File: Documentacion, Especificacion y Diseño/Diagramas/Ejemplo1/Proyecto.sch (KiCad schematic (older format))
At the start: 12 parts

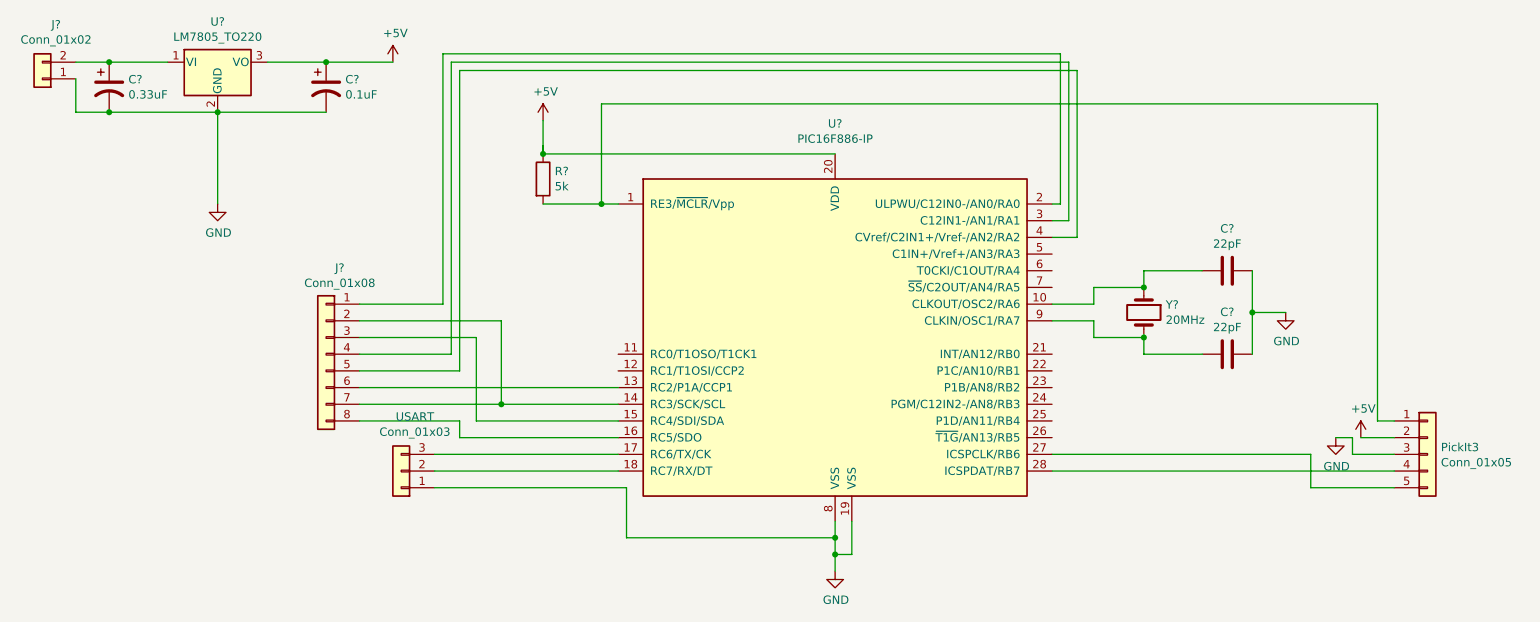
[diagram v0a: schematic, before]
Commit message: Tratado de hacer parte del circuito sin cruces y con especificaciones
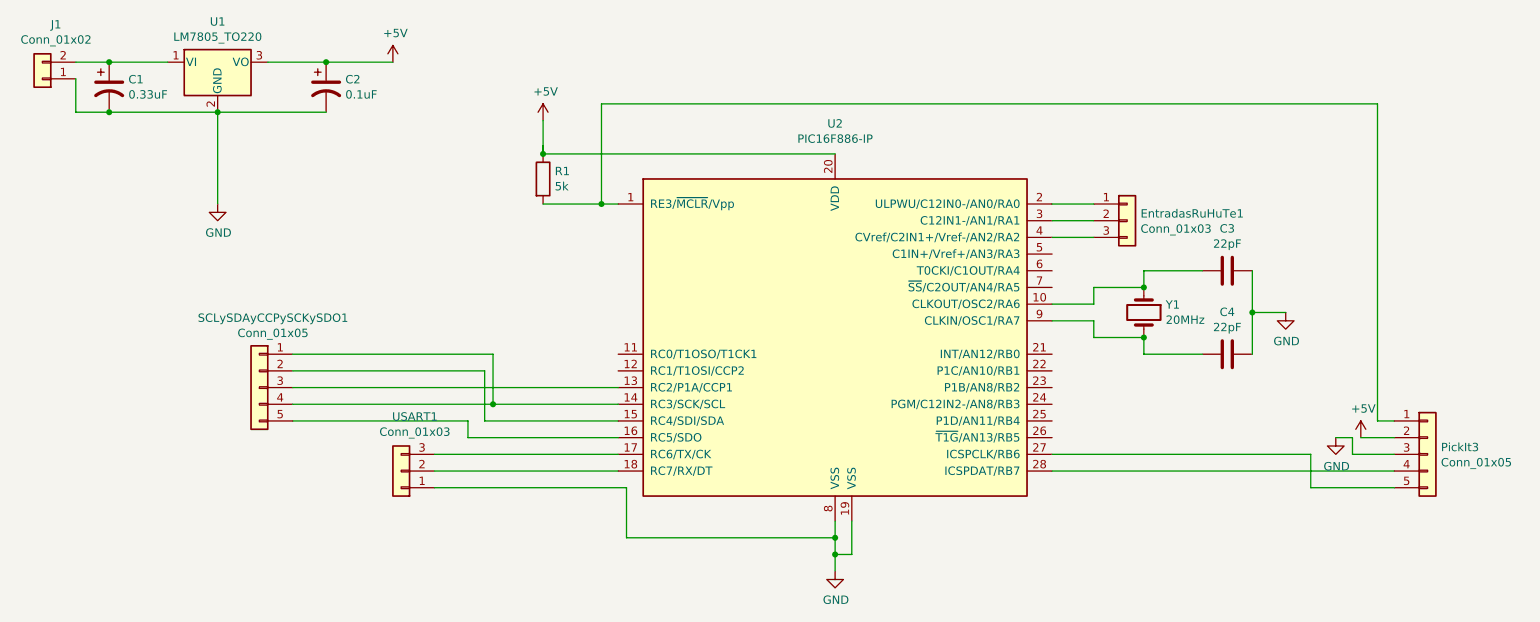
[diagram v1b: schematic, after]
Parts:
- removed J?: Conn_01x08, symbol Connector_Generic:Conn_01x08
- added EntradasRuHuTe1: Conn_01x03, Connector_PinHeader_2.54mm:PinHeader_1x03_P2.54mm_Vertical, symbol Connector_Generic:Conn_01x03
- added SCLySDAyCCPySCKySDO1: Conn_01x05, Connector_PinHeader_2.54mm:PinHeader_1x05_P2.54mm_Vertical, symbol Connector_Generic:Conn_01x05
- C1, C2: renamed from C?; footprint (none) -> Capacitor_THT:CP_Radial_D5.0mm_P2.50mm
- C3, C4: renamed from C?; footprint (none) -> Capacitor_THT:C_Disc_D5.0mm_W2.5mm_P2.50mm
- J1: renamed from J?; footprint (none) -> TerminalBlock:TerminalBlock_bornier-2_P5.08mm
- PickIt3: footprint (none) -> Connector_PinHeader_2.54mm:PinHeader_1x05_P2.54mm_Vertical
- R1: renamed from R?; footprint (none) -> Resistor_THT:R_Axial_DIN0204_L3.6mm_D1.6mm_P7.62mm_Horizontal
- U2: renamed from U?; footprint (none) -> Package_DIP:DIP-28_W7.62mm_LongPads
- USART1: renamed from USART; footprint (none) -> Connector_PinHeader_2.54mm:PinHeader_1x03_P2.54mm_Vertical
- Y1: renamed from Y?; footprint (none) -> Crystal:Crystal_HC18-U_Vertical
- gave numbers to parts that had none: 1
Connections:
- net at U2.13 (RC2/P1A/CCP1): now also SCLySDAyCCPySCKySDO1.3 (Pin_3)
- net at U2.14 (RC3/SCK/SCL): now also SCLySDAyCCPySCKySDO1.1 (Pin_1), SCLySDAyCCPySCKySDO1.4 (Pin_4)
- net at U2.15 (RC4/SDI/SDA): now also SCLySDAyCCPySCKySDO1.2 (Pin_2)
- net at U2.16 (RC5/SDO): now also SCLySDAyCCPySCKySDO1.5 (Pin_5)
- net at U2.2 (ULPWU/C12IN0-/AN0/RA0): now also EntradasRuHuTe1.1 (Pin_1)
- net at U2.3 (C12IN1-/AN1/RA1): now also EntradasRuHuTe1.2 (Pin_2)
- net at U2.4 (CVref/C2IN1+/Vref-/AN2/RA2): now also EntradasRuHuTe1.3 (Pin_3)
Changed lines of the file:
@@
 $EndDescr
 $Comp
-L MCU_Microchip_PIC16:PIC16F886-IP U?
+L MCU_Microchip_PIC16:PIC16F886-IP U2
 U 1 1 635A720F
 P 5750 3650
-F 0 "U?" H 5750 4931 50  0000 C CNN
+F 0 "U2" H 5750 4931 50  0000 C CNN
 F 1 "PIC16F886-IP" H 5750 4840 50  0000 C CNN
-F 2 "" H 5750 3650 50  0001 C CIN
+F 2 "Package_DIP:DIP-28_W7.62mm_LongPads" H 5750 3650 50  0001 C CIN
 F 3 "http://ww1.microchip.com/downloads/en/DeviceDoc/41291D.pdf" H 5750 3450 50  0001 C CNN
 	1    5750 3650
@@
 $EndComp
 $Comp
-L Regulator_Linear:LM7805_TO220 U?
+L Regulator_Linear:LM7805_TO220 U1
 U 1 1 635A980B
 P 2050 2000
-F 0 "U?" H 2050 2242 50  0000 C CNN
+F 0 "U1" H 2050 2242 50  0000 C CNN
 F 1 "LM7805_TO220" H 2050 2151 50  0000 C CNN
 F 2 "Package_TO_SOT_THT:TO-220-3_Vertical" H 2050 2225 50  0001 C CIN
@@
 $EndComp
 $Comp
-L Device:CP1 C?
+L Device:CP1 C1
 U 1 1 635AAA2C
 P 1400 2150
-F 0 "C?" H 1515 2196 50  0000 L CNN
+F 0 "C1" H 1515 2196 50  0000 L CNN
 F 1 "0.33uF" H 1515 2105 50  0000 L CNN
-F 2 "" H 1400 2150 50  0001 C CNN
+F 2 "Capacitor_THT:CP_Radial_D5.0mm_P2.50mm" H 1400 2150 50  0001 C CNN
 F 3 "~" H 1400 2150 50  0001 C CNN
 	1    1400 2150
@@
 $EndComp
 $Comp
-L Device:CP1 C?
+L Device:CP1 C2
 U 1 1 635AB87C
 P 2700 2150
-F 0 "C?" H 2815 2196 50  0000 L CNN
+F 0 "C2" H 2815 2196 50  0000 L CNN
 F 1 "0.1uF" H 2815 2105 50  0000 L CNN
-F 2 "" H 2700 2150 50  0001 C CNN
+F 2 "Capacitor_THT:CP_Radial_D5.0mm_P2.50mm" H 2700 2150 50  0001 C CNN
 F 3 "~" H 2700 2150 50  0001 C CNN
 	1    2700 2150
@@
 $EndComp
 $Comp
-L Connector_Generic:Conn_01x02 J?
+L Connector_Generic:Conn_01x02 J1
 U 1 1 635ACCCC
 P 1000 2100
-F 0 "J?" H 918 1775 50  0000 C CNN
+F 0 "J1" H 918 1775 50  0000 C CNN
 F 1 "Conn_01x02" H 918 1866 50  0000 C CNN
-F 2 "" H 1000 2100 50  0001 C CNN
+F 2 "TerminalBlock:TerminalBlock_bornier-2_P5.08mm" H 1000 2100 50  0001 C CNN
 F 3 "~" H 1000 2100 50  0001 C CNN
 	1    1000 2100
@@
 $EndComp
 $Comp
-L power:+5V #PWR?
+L power:+5V #PWR02
 U 1 1 635AFC36
 P 3100 2000
-F 0 "#PWR?" H 3100 1850 50  0001 C CNN
+F 0 "#PWR02" H 3100 1850 50  0001 C CNN
 F 1 "+5V" H 3115 2173 50  0000 C CNN
 F 2 "" H 3100 2000 50  0001 C CNN
@@
 $EndComp
 $Comp
-L power:GND #PWR?
+L power:GND #PWR01
 U 1 1 635B08D2
 P 2050 2850
-F 0 "#PWR?" H 2050 2600 50  0001 C CNN
+F 0 "#PWR01" H 2050 2600 50  0001 C CNN
 F 1 "GND" H 2055 2677 50  0000 C CNN
 F 2 "" H 2050 2850 50  0001 C CNN
@@
 Connection ~ 1400 2300
 $Comp
-L power:GND #PWR?
+L power:GND #PWR04
 U 1 1 635B28CF
 P 5750 5050
-F 0 "#PWR?" H 5750 4800 50  0001 C CNN
+F 0 "#PWR04" H 5750 4800 50  0001 C CNN
 F 1 "GND" H 5755 4877 50  0000 C CNN
 F 2 "" H 5750 5050 50  0001 C CNN
@@
 	5750 4950 5750 5050
 $Comp
-L Device:R R?
+L Device:R R1
 U 1 1 635B3A7F
 P 4000 2700
-F 0 "R?" H 4070 2746 50  0000 L CNN
+F 0 "R1" H 4070 2746 50  0000 L CNN
 F 1 "5k" H 4070 2655 50  0000 L CNN
-F 2 "" V 3930 2700 50  0001 C CNN
+F 2 "Resistor_THT:R_Axial_DIN0204_L3.6mm_D1.6mm_P7.62mm_Horizontal" V 3930 2700 50  0001 C CNN
 F 3 "~" H 4000 2700 50  0001 C CNN
 	1    4000 2700
@@
 $EndComp
 $Comp
-L power:+5V #PWR?
+L power:+5V #PWR03
 U 1 1 635B48DF
 P 4000 2350
-F 0 "#PWR?" H 4000 2200 50  0001 C CNN
+F 0 "#PWR03" H 4000 2200 50  0001 C CNN
 F 1 "+5V" H 4015 2523 50  0000 C CNN
 F 2 "" H 4000 2350 50  0001 C CNN
@@
 F 0 "PickIt3" H 9380 4392 50  0000 L CNN
 F 1 "Conn_01x05" H 9380 4301 50  0000 L CNN
-F 2 "" H 9300 4350 50  0001 C CNN
+F 2 "Connector_PinHeader_2.54mm:PinHeader_1x05_P2.54mm_Vertical" H 9300 4350 50  0001 C CNN
 F 3 "~" H 9300 4350 50  0001 C CNN
 	1    9300 4350
@@
 	4000 2350 4000 2550
 $Comp
-L power:+5V #PWR?
+L power:+5V #PWR07
 U 1 1 635C3E4F
 P 8900 4250
-F 0 "#PWR?" H 8900 4100 50  0001 C CNN
+F 0 "#PWR07" H 8900 4100 50  0001 C CNN
 F 1 "+5V" H 8915 4423 50  0000 C CNN
 F 2 "" H 8900 4250 50  0001 C CNN
@@
 $EndComp
 $Comp
-L power:GND #PWR?
+L power:GND #PWR06
 U 1 1 635C471C
 P 8750 4250
-F 0 "#PWR?" H 8750 4000 50  0001 C CNN
+F 0 "#PWR06" H 8750 4000 50  0001 C CNN
 F 1 "GND" H 8755 4077 50  0000 C CNN
 F 2 "" H 8750 4250 50  0001 C CNN
@@
 $EndComp
 $Comp
-L Connector_Generic:Conn_01x03 USART
+L Connector_Generic:Conn_01x03 USART1
 U 1 1 635CC670
 P 3150 4450
-F 0 "USART" H 3068 4125 50  0000 C CNN
+F 0 "USART1" H 3068 4125 50  0000 C CNN
 F 1 "Conn_01x03" H 3068 4216 50  0000 C CNN
-F 2 "" H 3150 4450 50  0001 C CNN
+F 2 "Connector_PinHeader_2.54mm:PinHeader_1x03_P2.54mm_Vertical" H 3150 4450 50  0001 C CNN
 F 3 "~" H 3150 4450 50  0001 C CNN
 	1    3150 4450
@@
 $EndComp
 $Comp
-L Device:Crystal Y?
+L Device:Crystal Y1
 U 1 1 635F31A4
 P 7600 3500
-F 0 "Y?" V 7554 3631 50  0000 L CNN
+F 0 "Y1" V 7554 3631 50  0000 L CNN
 F 1 "20MHz" V 7645 3631 50  0000 L CNN
-F 2 "" H 7600 3500 50  0001 C CNN
+F 2 "Crystal:Crystal_HC18-U_Vertical" H 7600 3500 50  0001 C CNN
 F 3 "~" H 7600 3500 50  0001 C CNN
 	1    7600 3500
@@
 $EndComp
 $Comp
-L Device:C C?
+L Device:C C3
 U 1 1 635F445D
 P 8100 3250
-F 0 "C?" V 7848 3250 50  0000 C CNN
+F 0 "C3" V 7848 3250 50  0000 C CNN
 F 1 "22pF" V 7939 3250 50  0000 C CNN
-F 2 "" H 8138 3100 50  0001 C CNN
+F 2 "Capacitor_THT:C_Disc_D5.0mm_W2.5mm_P2.50mm" H 8138 3100 50  0001 C CNN
 F 3 "~" H 8100 3250 50  0001 C CNN
 	1    8100 3250
@@
 $EndComp
 $Comp
-L Device:C C?
+L Device:C C4
 U 1 1 635F47D1
 P 8100 3750
-F 0 "C?" V 7848 3750 50  0000 C CNN
+F 0 "C4" V 7848 3750 50  0000 C CNN
 F 1 "22pF" V 7939 3750 50  0000 C CNN
-F 2 "" H 8138 3600 50  0001 C CNN
+F 2 "Capacitor_THT:C_Disc_D5.0mm_W2.5mm_P2.50mm" H 8138 3600 50  0001 C CNN
 F 3 "~" H 8100 3750 50  0001 C CNN
 	1    8100 3750
@@
 	7300 3550 7050 3550
 $Comp
-L power:GND #PWR?
+L power:GND #PWR05
 U 1 1 635FE965
 P 8450 3500
-F 0 "#PWR?" H 8450 3250 50  0001 C CNN
+F 0 "#PWR05" H 8450 3250 50  0001 C CNN
 F 1 "GND" H 8455 3327 50  0000 C CNN
 F 2 "" H 8450 3500 50  0001 C CNN
@@
 Wire Wire Line
 	5750 4850 5750 4950
-$Comp
-L Connector_Generic:Conn_01x08 J?
-U 1 1 635E679D
-P 2700 3750
-F 0 "J?" H 2618 4267 50  0000 C CNN
-F 1 "Conn_01x08" H 2618 4176 50  0000 C CNN
-F 2 "" H 2700 3750 50  0001 C CNN
-F 3 "~" H 2700 3750 50  0001 C CNN
-	1    2700 3750
+Wire Wire Line
+	2050 2300 2050 2850
+Wire Wire Line
+	2700 2300 2050 2300
+$Comp
+L Connector_Generic:Conn_01x05 SCLySDAyCCPySCKySDO1
+U 1 1 63641777
+P 2300 3950
+F 0 "SCLySDAyCCPySCKySDO1" H 2218 4367 50  0000 C CNN
+F 1 "Conn_01x05" H 2218 4276 50  0000 C CNN
+F 2 "Connector_PinHeader_2.54mm:PinHeader_1x05_P2.54mm_Vertical" H 2300 3950 50  0001 C CNN
+F 3 "~" H 2300 3950 50  0001 C CNN
+	1    2300 3950
 	-1   0    0    -1
 $EndComp
-Wire Wire Line
-	4450 4250 3500 4250
-Wire Wire Line
-	3500 4250 3500 4150
-Wire Wire Line
-	3500 4150 2900 4150
-Wire Wire Line
-	2900 3450 3400 3450
-Wire Wire Line
-	3400 3450 3400 1950
-Wire Wire Line
-	3400 1950 7100 1950
-Wire Wire Line
-	7100 1950 7100 2850
-Wire Wire Line
-	7100 2850 7050 2850
-Wire Wire Line
-	2900 4050 3750 4050
-Wire Wire Line
-	2900 3550 3750 3550
-Wire Wire Line
-	3750 3550 3750 4050
-Connection ~ 3750 4050
-Wire Wire Line
-	3750 4050 4450 4050
-Wire Wire Line
-	4450 4150 3600 4150
-Wire Wire Line
-	3600 4150 3600 3650
-Wire Wire Line
-	3600 3650 2900 3650
-Wire Wire Line
-	2900 3750 3450 3750
-Wire Wire Line
-	3450 3750 3450 2000
-Wire Wire Line
-	3450 2000 7150 2000
-Wire Wire Line
-	7150 2000 7150 2950
-Wire Wire Line
-	7150 2950 7050 2950
-Wire Wire Line
-	2900 3850 3500 3850
-Wire Wire Line
-	3500 3850 3500 2050
-Wire Wire Line
-	3500 2050 7200 2050
-Wire Wire Line
-	7200 2050 7200 3050
-Wire Wire Line
-	7200 3050 7050 3050
-Wire Wire Line
-	4450 3950 2900 3950
-Wire Wire Line
-	2050 2300 2050 2850
-Wire Wire Line
-	2700 2300 2050 2300
+$Comp
+L Connector_Generic:Conn_01x03 EntradasRuHuTe1
+U 1 1 636422CB
+P 7500 2950
+F 0 "EntradasRuHuTe1" H 7580 2992 50  0000 L CNN
+F 1 "Conn_01x03" H 7580 2901 50  0000 L CNN
+F 2 "Connector_PinHeader_2.54mm:PinHeader_1x03_P2.54mm_Vertical" H 7500 2950 50  0001 C CNN
+F 3 "~" H 7500 2950 50  0001 C CNN
+	1    7500 2950
+	1    0    0    -1
+$EndComp
+Wire Wire Line
+	7050 2850 7300 2850
+Wire Wire Line
+	7050 2950 7300 2950
+Wire Wire Line
+	7050 3050 7300 3050
+Wire Wire Line
+	4450 4250 3550 4250
+Wire Wire Line
+	3550 4250 3550 4150
+Wire Wire Line
+	3550 4150 2500 4150
+Wire Wire Line
+	4450 4150 3650 4150
+Wire Wire Line
+	3650 3850 2500 3850
+Wire Wire Line
+	3650 3850 3650 4150
+Wire Wire Line
+	3700 4050 3700 3750
+Wire Wire Line
+	3700 3750 2500 3750
+Wire Wire Line
+	3700 4050 4450 4050
+Wire Wire Line
+	3700 4050 2500 4050
+Connection ~ 3700 4050
+Wire Wire Line
+	4450 3950 2500 3950
 $EndSCHEMATC
